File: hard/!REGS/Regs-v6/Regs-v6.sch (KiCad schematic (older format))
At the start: 51 parts, among them J1 Conn_01x15_Female, J11 Conn_01x03_Male, J12 Conn_01x01_Male, J13 Conn_01x01_Male, J14 Conn_01x01_Male, J15 Conn_01x01_Male, J16 Screw_Terminal_01x02, J17 Conn_01x09_Male, J18 Conn_01x09_Male, J19 Conn_01x01_Male, J2 Conn_01x09_Male, J20 Conn_01x01_Male, J3 Conn_01x09_Male, J4 Conn_01x09_Male, J5 Conn_01x09_Male, J6 Conn_01x09_Male, J7 Conn_01x09_Male, J8 Conn_01x09_Male, Q1 IRLML5203, U1 REG_CNT, U10 REG_CNT, U11 REG_CNT, U12 REG_CNT, U13 74LS139, U14 74HC00, U15 MUX2-1, U16 REG_CNT, U17 REG_CNT, U18 REG_CNT, U19 REG_CNT, U2 REG_CNT, U3 REG_CNT, U4 REG_CNT, U5 REG_CNT, U6 REG_CNT, U7 REG_CNT, U8 REG_CNT, U9 REG_CNT

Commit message: Regs v6 in work
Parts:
- removed J2, J3, J4, J5, J6, J7, J8: Conn_01x09_Male, Connector_PinHeader_2.54mm:PinHeader_1x09_P2.54mm_Vertical, symbol Connector:Conn_01x09_Male
- added J2, J3, J4, J5, J6, J7, J8: Conn_01x15_Female, Connector_PinSocket_2.54mm:PinSocket_1x15_P2.54mm_Vertical, symbol Connector:Conn_01x15_Female
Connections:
- net R1.0: now also J2.1 (Pin_1)
- net R1.1: now also J2.3 (Pin_3)
- net R1.2: now also J2.5 (Pin_5)
- net R1.3: now also J2.7 (Pin_7)
- net R1.4: now also J2.9 (Pin_9)
- net R1.5: now also J2.11 (Pin_11)
- net R1.6: now also J2.13 (Pin_13)
- net R1.7: now also J2.15 (Pin_15)
- net R2.0: now also J3.1 (Pin_1)
- net R2.1: now also J3.3 (Pin_3)
- net R2.2: now also J3.5 (Pin_5)
- net R2.3: now also J3.7 (Pin_7)
- net R2.4: now also J3.9 (Pin_9)
- net R2.5: now also J3.11 (Pin_11)
- net R2.6: now also J3.13 (Pin_13)
- net R2.7: now also J3.15 (Pin_15)
- net R3.0: now also J4.1 (Pin_1)
- net R3.1: now also J4.3 (Pin_3)
- net R3.2: now also J4.5 (Pin_5)
- net R3.3: now also J4.7 (Pin_7)
- net R3.4: now also J4.9 (Pin_9)
- net R3.5: now also J4.11 (Pin_11)
- net R3.6: now also J4.13 (Pin_13)
- net R3.7: now also J4.15 (Pin_15)
- net R4.0: now also J5.1 (Pin_1)
- net R4.1: now also J5.3 (Pin_3)
- net R4.2: now also J5.5 (Pin_5)
- net R4.3: now also J5.7 (Pin_7)
- net R4.4: now also J5.9 (Pin_9)
- net R4.5: now also J5.11 (Pin_11)
- net R4.6: now also J5.13 (Pin_13)
- net R4.7: now also J5.15 (Pin_15)
- net R5.0: now also J6.1 (Pin_1)
- net R5.1: now also J6.3 (Pin_3)
- net R5.2: now also J6.5 (Pin_5)
- net R5.3: now also J6.7 (Pin_7)
- net R5.4: now also J6.9 (Pin_9)
- net R5.5: now also J6.11 (Pin_11)
- net R5.6: now also J6.13 (Pin_13)
- net R5.7: now also J6.15 (Pin_15)
- net R6.0: now also J7.1 (Pin_1)
- net R6.1: now also J7.3 (Pin_3)
- net R6.2: now also J7.5 (Pin_5)
- net R6.3: now also J7.7 (Pin_7)
- net R6.4: now also J7.9 (Pin_9)
- net R6.5: now also J7.11 (Pin_11)
- net R6.6: now also J7.13 (Pin_13)
- net R6.7: now also J7.15 (Pin_15)
- net R7.0: now also J8.1 (Pin_1)
- net R7.1: now also J8.3 (Pin_3)
- net R7.2: now also J8.5 (Pin_5)
- net R7.3: now also J8.7 (Pin_7)
- net R7.4: now also J8.9 (Pin_9)
- net R7.5: now also J8.11 (Pin_11)
- net R7.6: now also J8.13 (Pin_13)
- net R7.7: now also J8.15 (Pin_15)
- no-connect marks 9 -> 58

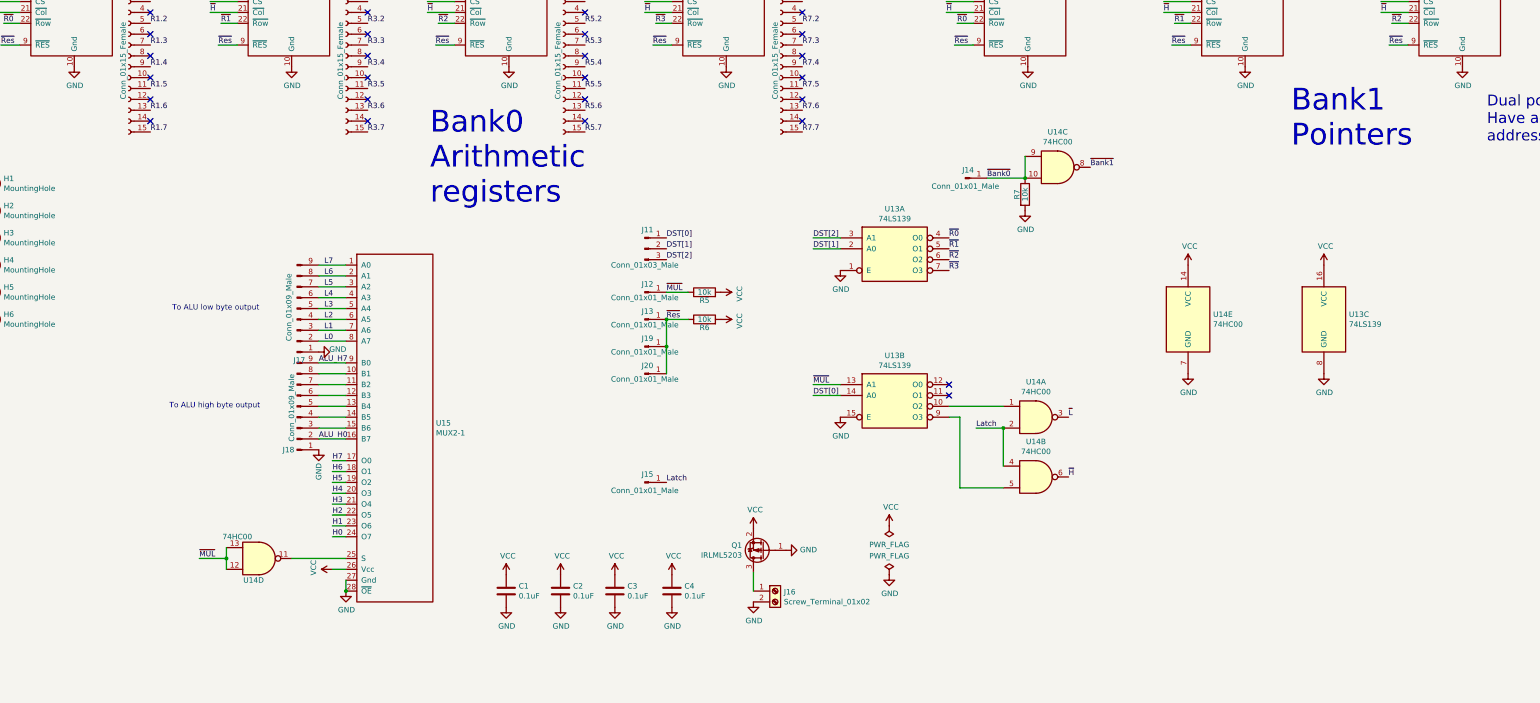
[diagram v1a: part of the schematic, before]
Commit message: Regs v6 pcb is almost ready
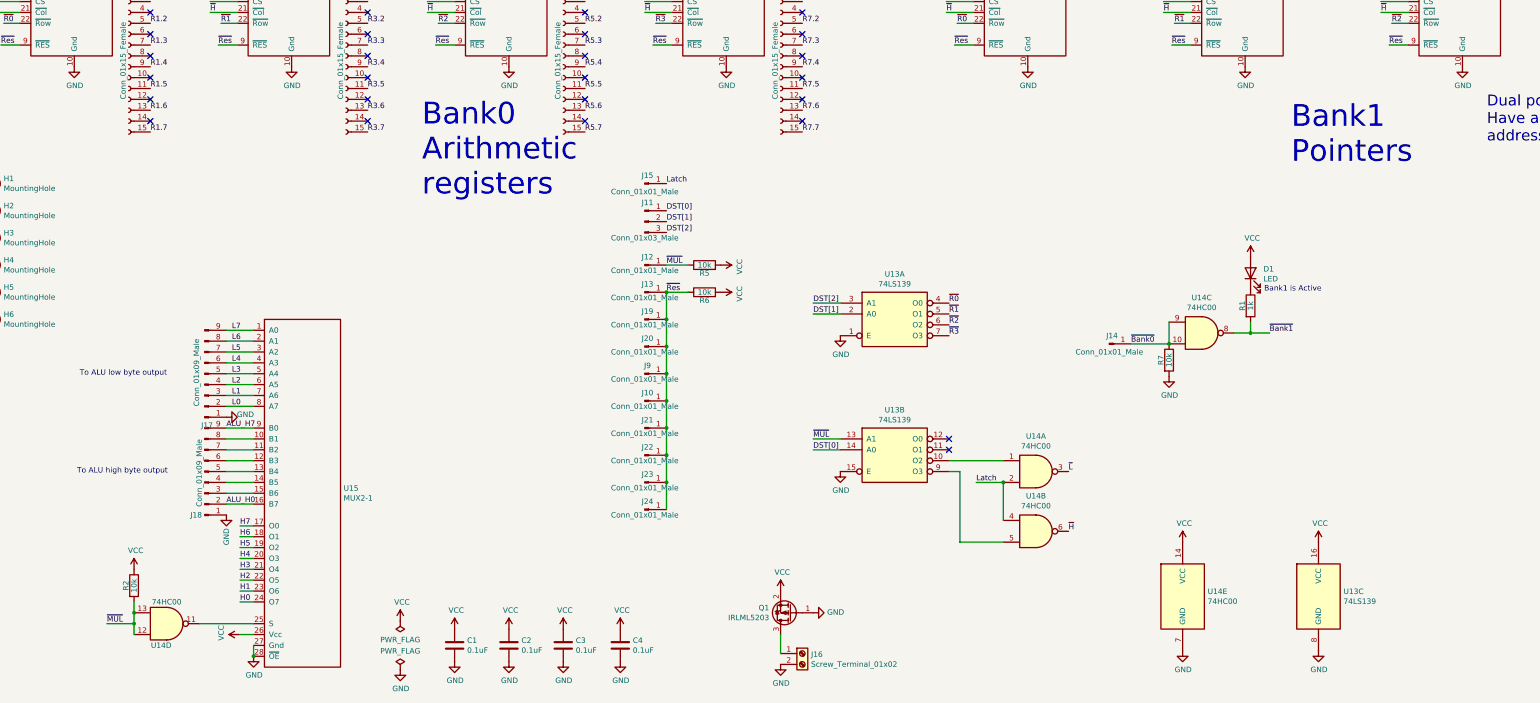
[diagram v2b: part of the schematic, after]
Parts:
- added D1: LED, LED_THT:LED_D5.0mm, symbol Device:LED
- added J10, J21, J22, J23, J24, J9: Conn_01x01_Male, Connector_PinHeader_2.54mm:PinHeader_1x01_P2.54mm_Vertical, symbol Connector:Conn_01x01_Male
- added R1: 1k, Resistor_SMD:R_0805_2012Metric_Pad1.20x1.40mm_HandSolder, symbol Device:R
- added R2: 10k, Resistor_SMD:R_0805_2012Metric_Pad1.20x1.40mm_HandSolder, symbol Device:R
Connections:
- net VCC: now also D1.2 (A), R2.1
- net ~Bank1: now also R1.2
- net ~MUL: now also R2.2
- net ~Res: now also J10.1 (Pin_1), J21.1 (Pin_1), J22.1 (Pin_1), J23.1 (Pin_1), J24.1 (Pin_1), J9.1 (Pin_1)
- new net: D1.1 (K), R1.1
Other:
- note added: "Bank1 is Active"
- moved on the sheet: C1, C2, C3, C4, J11, J12, J13, J14, J15, J16, J17, J18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
